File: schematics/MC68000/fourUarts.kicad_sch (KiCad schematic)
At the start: 46 parts, among them J3 RS232_1, J4 RS232_1, J5 RS232_1, J6 RS232_1, J7 Conn_02x20_Counter_Clockwise, J8 Conn_02x04_Counter_Clockwise, J9 Conn_02x02_Counter_Clockwise, U18_C1 100nf, U18_C2 100nf, U18_C3 100nf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

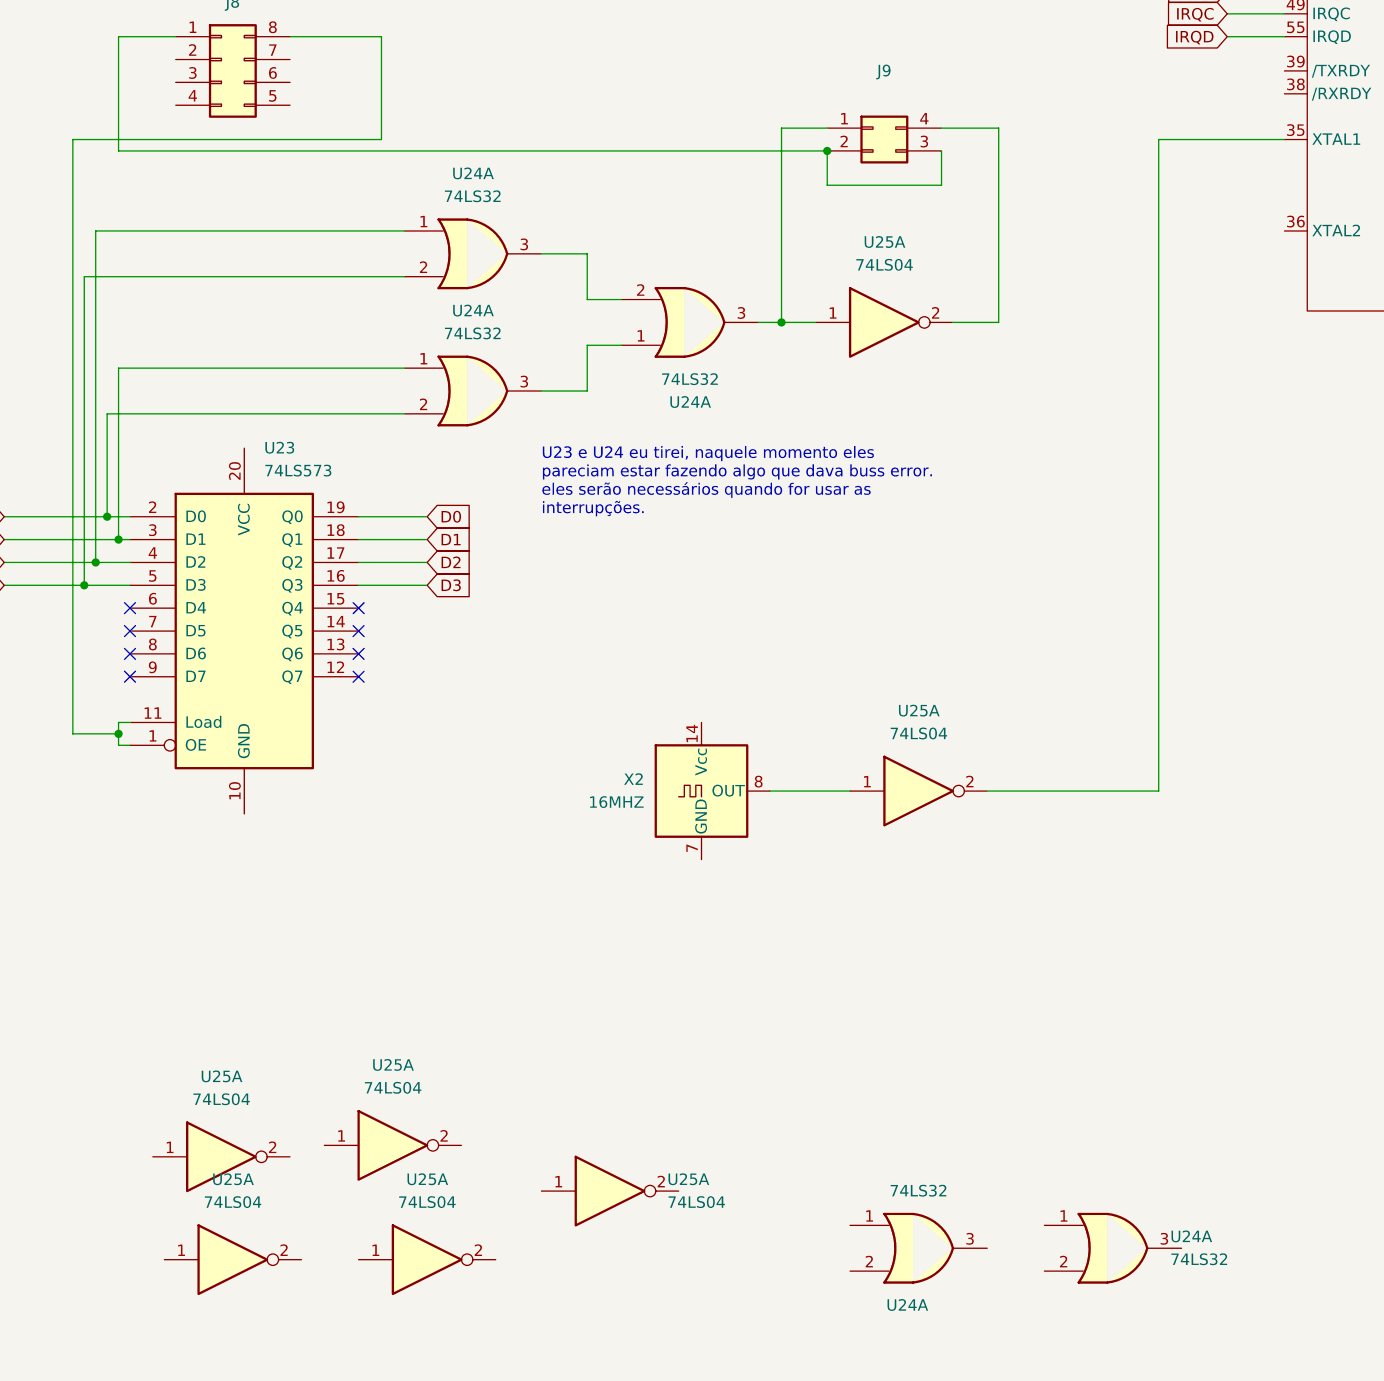
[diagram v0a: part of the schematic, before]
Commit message: Added ch376s
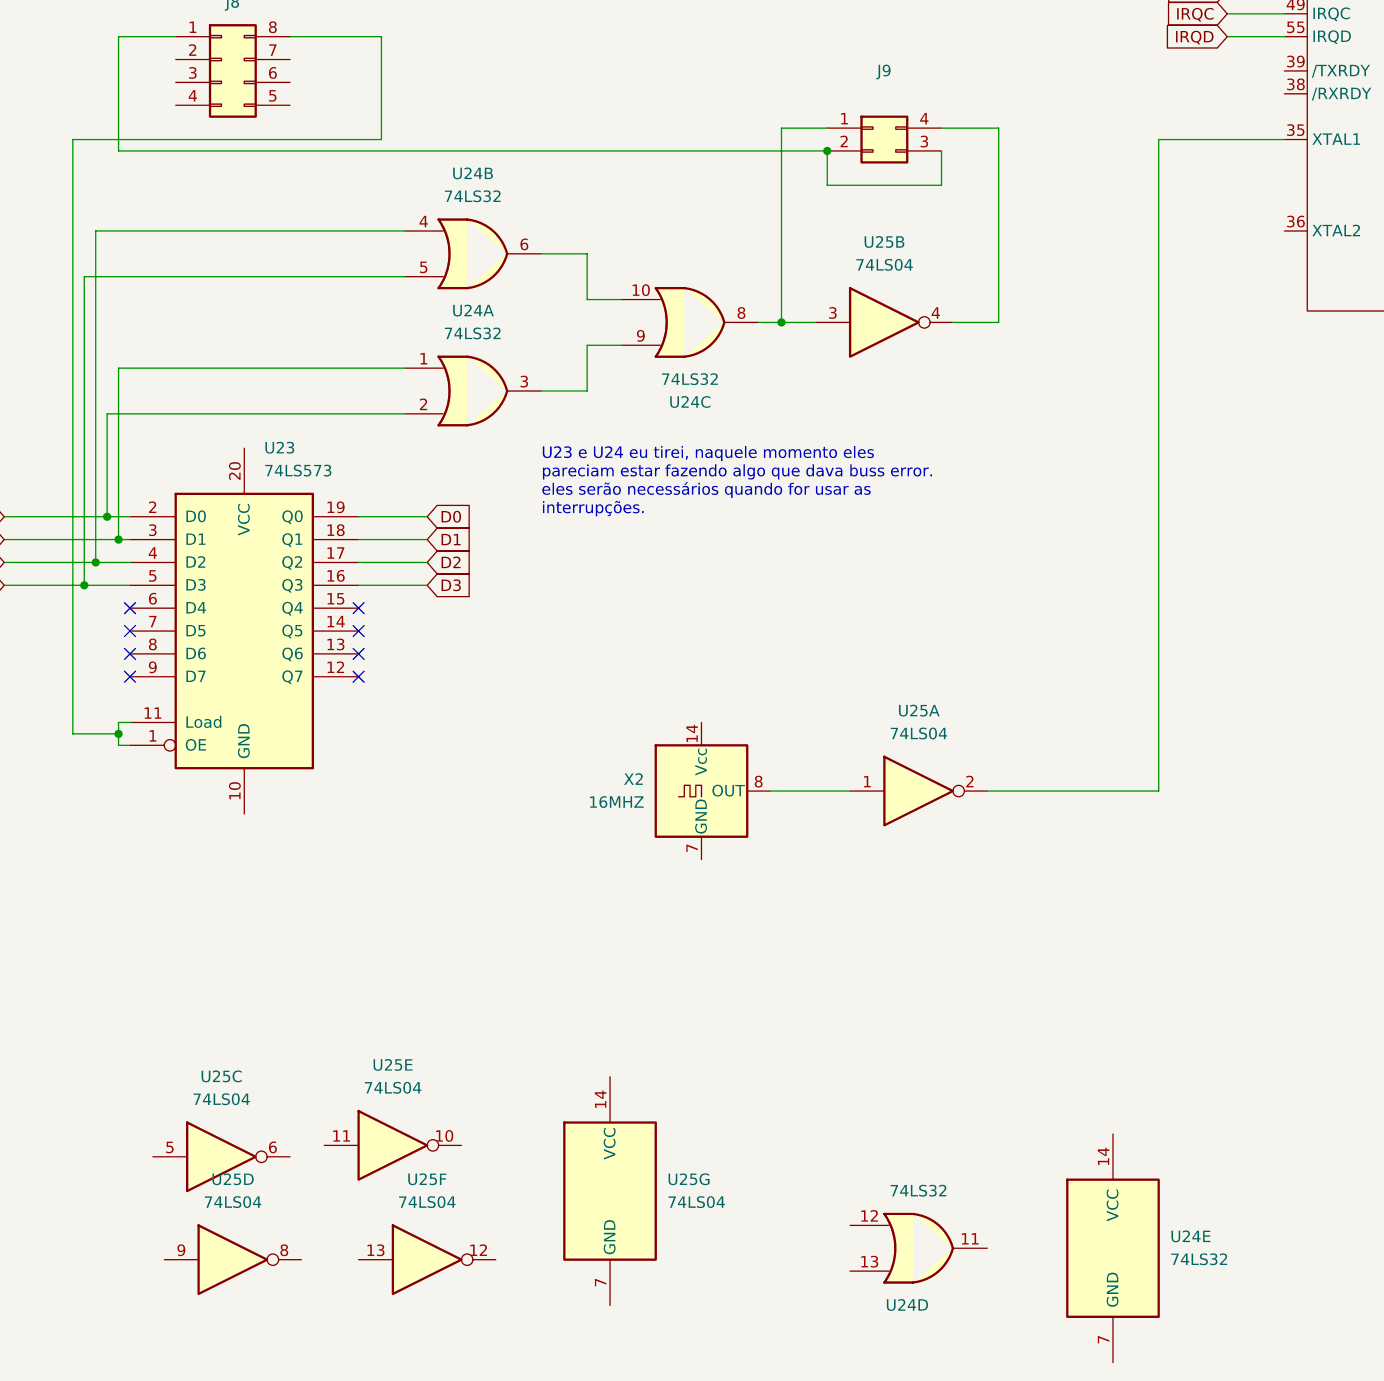
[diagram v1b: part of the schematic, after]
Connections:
- net IRQC: now also U24.5; no longer U24.2
- net IRQD: now also U24.4; no longer U24.1
- net at U24.3: now also U24.9; no longer U24.1
- net at J9.4 (Pin_4): now also U25.4; no longer U25.2
- new net: U24.10, U24.6
- new net: J9.1 (Pin_1), U24.8, U25.3
